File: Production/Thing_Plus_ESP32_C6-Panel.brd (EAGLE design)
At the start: 89.7 x 72.6 mm, 363 parts, among them J1 THING_PLUS_LOGICAL, J10 MICRO-SDFRICTION, J11 THING_PLUS_LOGICAL, J14 QWIIC_RIGHT_ANGLE, J15 MICRO-SDFRICTION, J4 QWIIC_RIGHT_ANGLE, J5 MICRO-SDFRICTION, J6 THING_PLUS_LOGICAL, J9 QWIIC_RIGHT_ANGLE, Q1 20V/4.2A/52mΩ/1.4W, Q2 20V/4.2A/52mΩ/1.4W, Q3 20V/4.2A/52mΩ/1.4W, Q4 20V/4.2A/52mΩ/1.4W, Q5 20V/4.2A/52mΩ/1.4W, Q6 20V/4.2A/52mΩ/1.4W, U1 ESP32-C6-WROOM-1-NARROW, U10 RT9080-33GJ5, U11 MCP73831, U12 MAX17048, U2 RT9080-33GJ5, U3 MCP73831, U4 MAX17048, U5 ESP32-C6-WROOM-1-NARROW, U6 RT9080-33GJ5, U7 MCP73831, U8 MAX17048, U9 ESP32-C6-WROOM-1-NARROW

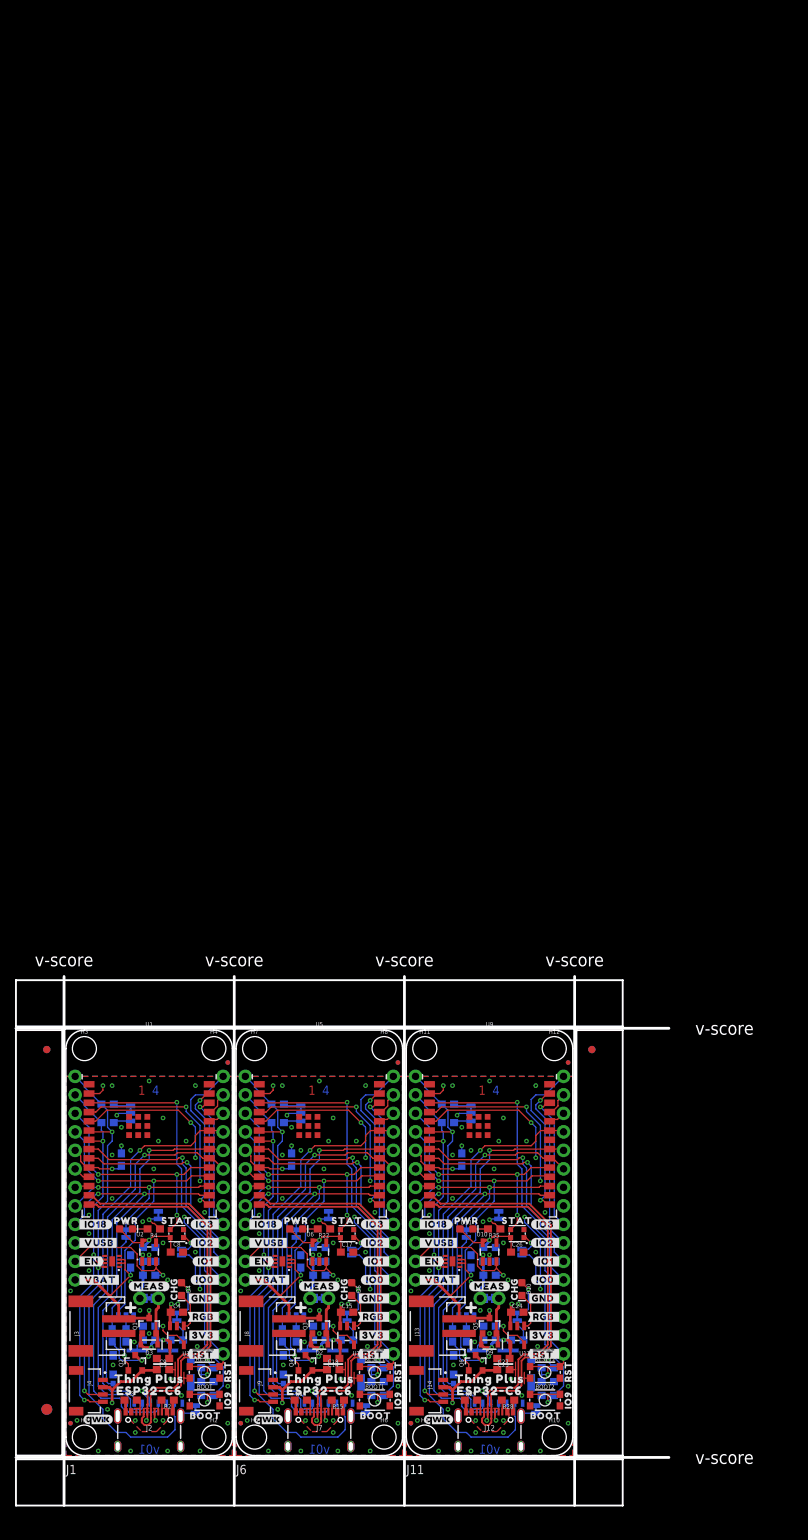
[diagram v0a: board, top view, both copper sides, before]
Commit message: Add v10 panel files
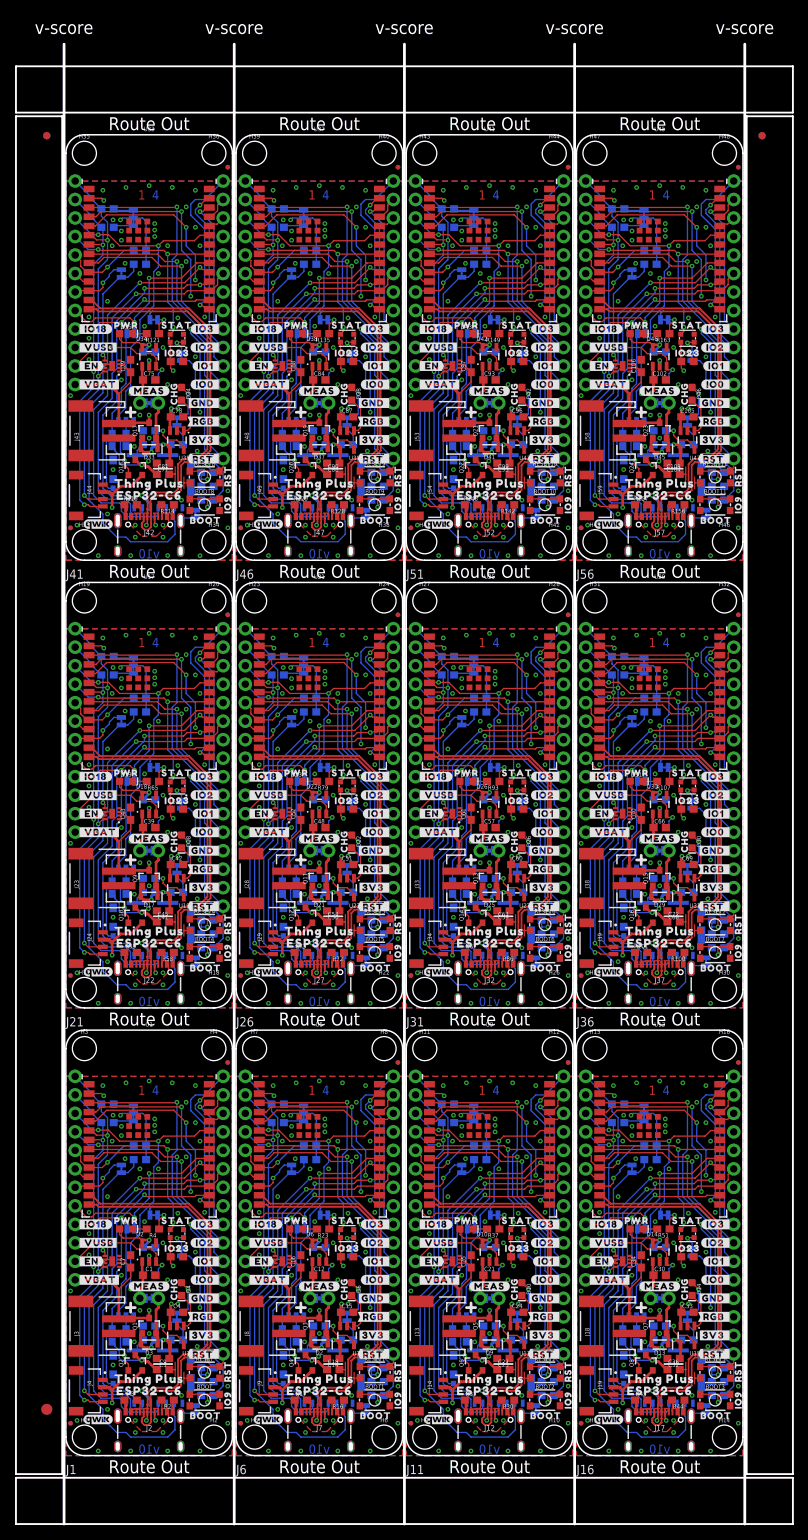
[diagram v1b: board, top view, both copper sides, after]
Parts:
- added ALRT, ALRT1, ALRT10, ALRT11, ALRT2, ALRT3, ALRT4, ALRT5, ALRT6, ALRT7, ALRT8, ALRT9, CHG10, CHG11, CHG3, CHG4, CHG5, CHG6, CHG7, CHG8, CHG9, PWR10, PWR11, PWR3, PWR4, PWR5, PWR6, PWR7, PWR8, PWR9, RGB10, RGB11, RGB3, RGB4, RGB5, RGB6, RGB7, RGB8, RGB9, SD_DET10, SD_DET11, SD_DET3, SD_DET4, SD_DET5, SD_DET6, SD_DET7, SD_DET8, SD_DET9, SHLD10, SHLD11, SHLD3, SHLD4, SHLD5, SHLD6, SHLD7, SHLD8, SHLD9: JUMPER-SMT_2_NC_TRACE_SILK, SparkFun-Jumpers:SMT-JUMPER_2_NC_TRACE_SILK
- added BOOT10, BOOT11, BOOT3, BOOT4, BOOT5, BOOT6, BOOT7, BOOT8, BOOT9, RESET10, RESET11, RESET3, RESET4, RESET5, RESET6, RESET7, RESET8, RESET9: MOMENTARY-SWITCH-SPST-SMD-4.6X2.8MM, SparkFun-Switches:TACTILE_SWITCH_SMD_4.6X2.8MM
- added C100, C101, C106, C107, C28, C29, C34, C35, C37, C38, C43, C44, C46, C47, C52, C53, C55, C56, C61, C62, C64, C65, C70, C71, C73, C74, C79, C80, C82, C83, C88, C89, C91, C92, C97, C98: 0.1uF, SparkFun-Capacitors:0603
- added C102, C103, C104, C105, C30, C31, C32, C33, C39, C40, C41, C42, C48, C49, C50, C51, C57, C58, C59, C60, C66, C67, C68, C69, C75, C76, C77, C78, C84, C85, C86, C87, C93, C94, C95, C96: 2.2uF, SparkFun-Capacitors:0603
- added C108, C36, C45, C54, C63, C72, C81, C90, C99: 10uF, SparkFun-Capacitors:0603
- added D13, D17, D21, D25, D29, D33, D37, D41, D45: 1A/23V/620mV, SparkFun-DiscreteSemi:SOD-323
- added D14, D18, D22, D26, D30, D34, D38, D42, D46: Yellow, SparkFun-LED:LED-0603
- added D15, D19, D23, D27, D31, D35, D39, D43, D47: (no value), SparkFun-LED:LED-0603
- added D16, D20, D24, D28, D32, D36, D40, D44, D48: WS2812_2020, SparkFun-LED:WS2812-2020
- added FD13, FD14, FD15, FD16, FD17, FD18, FD19, FD20, FD21, FD22, FD23, FD24, FD25, FD26, FD27, FD28, FD29, FD30, FD31, FD32, FD33, FD34, FD35, FD36, FD37, FD38, FD39, FD40, FD41, FD42, FD43, FD44, FD45, FD46, FD47, FD48: FIDUCIALUFIDUCIAL, SparkFun-Aesthetics:FIDUCIAL-MICRO
- added H13, H14, H15, H16, H17, H18, H19, H20, H21, H22, H23, H24, H25, H26, H27, H28, H29, H30, H31, H32, H33, H34, H35, H36, H37, H38, H39, H40, H41, H42, H43, H44, H45, H46, H47, H48: STAND-OFF, SparkFun-Hardware:STAND-OFF
- added I2C10, I2C11, I2C3, I2C4, I2C5, I2C6, I2C7, I2C8, I2C9: JUMPER-SMT_3_2-NC_TRACE_SILK, SparkFun-Jumpers:SMT-JUMPER_3_2-NC_TRACE_SILK
- added J16, J21, J26, J31, J36, J41, J46, J51, J56: THING_PLUS_LOGICAL, SparkFun-Boards:THING_PLUS
- added J17, J22, J27, J32, J37, J42, J47, J52, J57: (no value), SparkFun-Connectors:USB-C-16P_4LAYER-PADS
- added J18, J23, J28, J33, J38, J43, J48, J53, J58: (no value), SparkFun-Connectors:JST-2-SMD
- added J19, J24, J29, J34, J39, J44, J49, J54, J59: QWIIC_RIGHT_ANGLE, SparkFun-Connectors:JST04_1MM_RA
- added J20, J25, J30, J35, J40, J45, J50, J55, J60: MICRO-SDFRICTION, SparkFun-Connectors:MICROSD_TINY
- added LOGO10, LOGO13, LOGO16, LOGO19, LOGO22, LOGO25, LOGO28, LOGO31, LOGO34: SFE_LOGO_NAME_FLAME.1_INCH, SparkFun-Aesthetics:SFE_LOGO_NAME_FLAME_.1
- added LOGO11, LOGO14, LOGO17, LOGO20, LOGO23, LOGO26, LOGO29, LOGO32, LOGO35: QWIIC_LOGO_4MM, SparkFun-Aesthetics:QWIIC_4MM
- added LOGO12, LOGO15, LOGO18, LOGO21, LOGO24, LOGO27, LOGO30, LOGO33, LOGO36: OSHW-LOGOM, SparkFun-Aesthetics:OSHW-LOGO-M
- added LP10, LP11, LP3, LP4, LP5, LP6, LP7, LP8, LP9: JUMPER-SMT_3_1-NC_TRACE_SILK, SparkFun-Jumpers:SMT-JUMPER_3_1-NC_TRACE_SILK
- added MEAS10, MEAS11, MEAS3, MEAS4, MEAS5, MEAS6, MEAS7, MEAS8, MEAS9: JUMPER-COMBO_2_NC_TRACE, SparkFun-Jumpers:COMBO-JUMPER_2_NC_TRACE
- added Q10, Q11, Q12, Q13, Q14, Q15, Q16, Q17, Q18, Q19, Q20, Q21, Q22, Q23, Q24, Q7, Q8, Q9: 20V/4.2A/52mΩ/1.4W, SparkFun-DiscreteSemi:SOT23-3
- added R100, R101, R114, R115, R128, R129, R142, R143, R156, R157, R44, R45, R58, R59, R72, R73, R86, R87: 5.1k, SparkFun-Resistors:0603
- added R102, R103, R104, R110, R111, R112, R113, R116, R117, R118, R124, R125, R126, R127, R130, R131, R132, R138, R139, R140, R141, R144, R145, R146, R152, R153, R154, R155, R158, R159, R160, R166, R167, R168, R40, R41, R42, R43, R46, R47, R48, R54, R55, R56, R57, R60, R61, R62, R68, R69, R70, R71, R74, R75, R76, R82, R83, R84, R85, R88, R89, R90, R96, R97, R98, R99: 100k, SparkFun-Resistors:0603
- added R105, R106, R107, R119, R120, R121, R133, R134, R135, R147, R148, R149, R161, R162, R163, R49, R50, R51, R63, R64, R65, R77, R78, R79, R91, R92, R93: 4.7k, SparkFun-Resistors:0603
- added R108, R109, R122, R123, R136, R137, R150, R151, R164, R165, R52, R53, R66, R67, R80, R81, R94, R95: 2.2k, SparkFun-Resistors:0603
- added U$184, U$247, U$310, U$373, U$436, U$499, U$562, U$625, U$688, U$751: (no value), output:#_IO21#POCI#0
- added U$185, U$248, U$311, U$374, U$437, U$500, U$563, U$626, U$689, U$752: (no value), output:#_IO19#SCK#0
- added U$186, U$249, U$312, U$375, U$438, U$501, U$564, U$627, U$690, U$753: (no value), output:#_IO20#PICO#0
- added U$187, U$250, U$313, U$376, U$439, U$502, U$565, U$628, U$691, U$754: (no value), output:#LP#0
- added U$188, U$251, U$314, U$377, U$440, U$503, U$566, U$629, U$692, U$755: (no value), output:#IO15#0
- added U$189, U$252, U$315, U$378, U$441, U$504, U$567, U$630, U$693, U$756: (no value), output:#ALRT#0
- added U$190, U$253, U$316, U$379, U$442, U$505, U$568, U$631, U$694: (no value), output:#SHLD#0
- added U$191, U$254, U$317, U$380, U$443, U$506, U$569, U$632, U$695: (no value), output:#I�C#0
- added U$192, U$255, U$318, U$381, U$444, U$507, U$570, U$633, U$696: (no value), output:#_IO18#0
- added U$193, U$256, U$319, U$382, U$445, U$508, U$571, U$634, U$697: (no value), output:#_VUSB#0
- added U$194, U$257, U$320, U$383, U$446, U$509, U$572, U$635, U$698: (no value), output:#_VBAT#0
- added U$195, U$258, U$321, U$384, U$447, U$510, U$573, U$636, U$699: (no value), output:#_EN#0
- added U$196, U$259, U$322, U$385, U$448, U$511, U$574, U$637, U$700: (no value), output:#IO3_#0
- added U$197, U$260, U$323, U$386, U$449, U$512, U$575, U$638, U$701: (no value), output:#IO2_#0
- added U$198, U$261, U$324, U$387, U$450, U$513, U$576, U$639, U$702: (no value), output:#IO1_#0
- added U$199, U$262, U$325, U$388, U$451, U$514, U$577, U$640, U$703: (no value), output:#IO0_#0
- added U$200, U$263, U$326, U$389, U$452, U$515, U$578, U$641, U$704: (no value), output:#GND_#0
- added U$201, U$264, U$327, U$390, U$453, U$516, U$579, U$642, U$705: (no value), output:#3V3_#0
- added U$202, U$223, U$265, U$286, U$328, U$349, U$391, U$412, U$454, U$475, U$517, U$538, U$580, U$601, U$643, U$664, U$706, U$727: (no value), output:##RST#_#0
- added U$203, U$266, U$329, U$392, U$455, U$518, U$581, U$644, U$707: (no value), output:#SDA#IO6_#0
- added U$204, U$267, U$330, U$393, U$456, U$519, U$582, U$645, U$708: (no value), output:#SCL#IO7_#0
- added U$205, U$268, U$331, U$394, U$457, U$520, U$583, U$646, U$709: (no value), output:#IO8_#0
- added U$206, U$269, U$332, U$395, U$458, U$521, U$584, U$647, U$710: (no value), output:#IO10_#0
- added U$207, U$270, U$333, U$396, U$459, U$522, U$585, U$648, U$711: (no value), output:#IO11_#0
- added U$208, U$271, U$334, U$397, U$460, U$523, U$586, U$649, U$712: (no value), output:#IO18_#0
- added U$209, U$272, U$335, U$398, U$461, U$524, U$587, U$650, U$713: (no value), output:#_IO9#0
- added U$210, U$273, U$336, U$399, U$462, U$525, U$588, U$651, U$714: (no value), output:#_IO16#TX#0
- added U$211, U$274, U$337, U$400, U$463, U$526, U$589, U$652, U$715: (no value), output:#_IO17#RX#0
- added U$212, U$275, U$338, U$401, U$464, U$527, U$590, U$653, U$716: (no value), output:#_IO5#0
- added U$213, U$276, U$339, U$402, U$465, U$528, U$591, U$654, U$717: (no value), output:#_IO4#0
- added U$214, U$277, U$340, U$403, U$466, U$529, U$592, U$655, U$718: (no value), output:#_IO3#0
- added U$215, U$278, U$341, U$404, U$467, U$530, U$593, U$656, U$719: (no value), output:#_IO2#0
- added U$216, U$279, U$342, U$405, U$468, U$531, U$594, U$657, U$720: (no value), output:#_IO1#0
- added U$217, U$280, U$343, U$406, U$469, U$532, U$595, U$658, U$721: (no value), output:#_IO0#0
- added U$218, U$281, U$344, U$407, U$470, U$533, U$596, U$659, U$722: (no value), output:#_GND#0
- added U$219, U$282, U$345, U$408, U$471, U$534, U$597, U$660, U$723: (no value), output:#_3V3#0
- added U$220, U$283, U$346, U$409, U$472, U$535, U$598, U$661, U$724: (no value), output:#VUSB_#0
- added U$221, U$284, U$347, U$410, U$473, U$536, U$599, U$662, U$725: (no value), output:#VBAT_#0
- added U$222, U$285, U$348, U$411, U$474, U$537, U$600, U$663, U$726: (no value), output:#EN_#0
- added U$224, U$287, U$350, U$413, U$476, U$539, U$602, U$665, U$728: (no value), output:#SD_DET#0
- added U$225, U$288, U$351, U$414, U$477, U$540, U$603, U$666, U$729: (no value), output:BOOT0
- added U$226, U$289, U$352, U$415, U$478, U$541, U$604, U$667, U$730: (no value), output:RST0
- added U$227, U$290, U$353, U$416, U$479, U$542, U$605, U$668, U$731: (no value), output:IO90
- added U$228, U$230, U$291, U$293, U$354, U$356, U$417, U$419, U$480, U$482, U$543, U$545, U$606, U$608, U$669, U$671, U$732, U$734: (no value), output:THING_PLUS0
- added U$229, U$231, U$292, U$294, U$355, U$357, U$418, U$420, U$481, U$483, U$544, U$546, U$607, U$609, U$670, U$672, U$733, U$735: (no value), output:ESP32#C60
- added U$232, U$233, U$295, U$296, U$358, U$359, U$421, U$422, U$484, U$485, U$547, U$548, U$610, U$611, U$673, U$674, U$736, U$737: (no value), output:#MEAS#0
- added U$234, U$297, U$360, U$423, U$486, U$549, U$612, U$675, U$738: (no value), output:#CHG#0
- added U$235, U$298, U$361, U$424, U$487, U$550, U$613, U$676, U$739: (no value), output:#PWR#0
- added U$236, U$299, U$362, U$425, U$488, U$551, U$614, U$677, U$740: (no value), output:PWR0
- added U$237, U$300, U$363, U$426, U$489, U$552, U$615, U$678, U$741: (no value), output:CHG0
- added U$238, U$301, U$364, U$427, U$490, U$553, U$616, U$679, U$742: (no value), output:STAT0
- added U$239, U$302, U$365, U$428, U$491, U$554, U$617, U$680, U$743: (no value), output:#RGB#0
- added U$240, U$303, U$366, U$429, U$492, U$555, U$618, U$681, U$744: (no value), output:#RGB_#0
- added U$241, U$304, U$367, U$430, U$493, U$556, U$619, U$682, U$745: (no value), output:#_RGB#0
- added U$242, U$305, U$368, U$431, U$494, U$557, U$620, U$683, U$746: (no value), output:#G#0
- added U$243, U$306, U$369, U$432, U$495, U$558, U$621, U$684, U$747: (no value), output:IO230
- added U$244, U$307, U$370, U$433, U$496, U$559, U$622, U$685, U$748: (no value), output:#IO15_#0
- added U$245, U$308, U$371, U$434, U$497, U$560, U$623, U$686, U$749: (no value), output:#IO23_#0
- added U$246, U$309, U$372, U$435, U$498, U$561, U$624, U$687, U$750: (no value), output:#IO22_#0
- added U13, U17, U21, U25, U29, U33, U37, U41, U45: ESP32-C6-WROOM-1-NARROW, ESP32-C6-WROOM-1:ESP32-C6-WROOM-1-NARROW
- added U14, U18, U22, U26, U30, U34, U38, U42, U46: RT9080-33GJ5, SparkFun-IC-Power:SOT23-5
- added U15, U19, U23, U27, U31, U35, U39, U43, U47: MCP73831, SparkFun-IC-Power:SOT23-5
- added U16, U20, U24, U28, U32, U36, U40, U44, U48: MAX17048, SparkFun-IC-Power:DFN-8
- R15, R28, R29: value 5.1k -> 100k
- R17, R30, R31: value 100k -> 5.1k
- R20, R33, R34: value 4.7k -> 100k
- R23, R36, R37: value 2.2k -> 4.7k
- R25, R38, R39: value 100k -> 2.2k
- RGB, RGB1, RGB2: value JUMPER-SMT_2_NO_SILK -> JUMPER-SMT_2_NC_TRACE_SILK; device SparkFun-Jumpers:SMT-JUMPER_2_NO_SILK -> SparkFun-Jumpers:SMT-JUMPER_2_NC_TRACE_SILK
- U$100: device output:#EN_#0 -> output:RST0
- U$101: device output:##RST#_#0 -> output:IO90
- U$102: device output:#SD_DET#0 -> output:THING_PLUS0
- U$103: device output:BOOT0 -> output:ESP32#C60
- U$104, U$165: device output:RST0 -> output:THING_PLUS0
- U$105, U$166: device output:IO90 -> output:ESP32#C60
- U$106, U$169: device output:THING_PLUS0 -> output:#MEAS#0
- U$107, U$170: device output:ESP32#C60 -> output:#MEAS#0
- U$108: device output:THING_PLUS0 -> output:#CHG#0
- U$109: device output:ESP32#C60 -> output:#PWR#0
- U$110: device output:#MEAS#0 -> output:PWR0
- U$111: device output:#MEAS#0 -> output:CHG0
- U$112: device output:#CHG#0 -> output:STAT0
- U$113: device output:#PWR#0 -> output:#RGB#0
- U$114: device output:PWR0 -> output:#RGB_#0
- U$115: device output:CHG0 -> output:#_RGB#0
- U$116: device output:STAT0 -> output:#G#0
- U$117: device output:#RGB#0 -> output:IO230
- U$118: device output:#RGB_#0 -> output:#IO15_#0
- U$119: device output:#_RGB#0 -> output:#IO23_#0
- U$120: device output:#SD_P#0 -> output:#IO22_#0
- U$121: device output:#IO20#0 -> output:#_IO21#POCI#0
- U$122: device output:#G#0 -> output:#_IO19#SCK#0
- U$123: device output:#SHLD#0 -> output:#_IO20#PICO#0
- U$124: device output:#I�C#0 -> output:#LP#0
- U$125: device output:#_IO18#0 -> output:#IO15#0
- U$126: device output:#_VUSB#0 -> output:#ALRT#0
- U$127: device output:#_VBAT#0 -> output:#SHLD#0
- U$128: device output:#_EN#0 -> output:#I�C#0
- U$129: device output:#IO3_#0 -> output:#_IO18#0
- U$130: device output:#IO2_#0 -> output:#_VUSB#0
- U$131: device output:#IO1_#0 -> output:#_VBAT#0
- U$132: device output:#IO0_#0 -> output:#_EN#0
- U$133: device output:#GND_#0 -> output:#IO3_#0
- U$134: device output:#3V3_#0 -> output:#IO2_#0
- U$135: device output:##RST#_#0 -> output:#IO1_#0
- U$136: device output:#SDA#IO6_#0 -> output:#IO0_#0
- U$137: device output:#SCL#IO7_#0 -> output:#GND_#0
- U$138: device output:#IO21_#0 -> output:#3V3_#0
- U$139: device output:#IO20_#0 -> output:##RST#_#0
- U$140: device output:#IO8_#0 -> output:#SDA#IO6_#0
- U$141: device output:#IO10_#0 -> output:#SCL#IO7_#0
- U$142: device output:#IO11_#0 -> output:#IO8_#0
- U$143: device output:#IO19_#0 -> output:#IO10_#0
- U$144: device output:#IO18_#0 -> output:#IO11_#0
- U$145: device output:#_IO9#0 -> output:#IO18_#0
- U$146: device output:#_IO16#TX#0 -> output:#_IO9#0
- U$147: device output:#_IO17#RX#0 -> output:#_IO16#TX#0
- U$148: device output:#_IO15#POCI#0 -> output:#_IO17#RX#0
- U$149: device output:#_IO23#PICO#0 -> output:#_IO5#0
- U$150: device output:#_IO22#SCK#0 -> output:#_IO4#0
- U$151: device output:#_IO5#0 -> output:#_IO3#0
- U$152: device output:#_IO4#0 -> output:#_IO2#0
- U$153: device output:#_IO3#0 -> output:#_IO1#0
- U$154: device output:#_IO2#0 -> output:#_IO0#0
- U$155: device output:#_IO1#0 -> output:#_GND#0
- U$156: device output:#_IO0#0 -> output:#_3V3#0
- U$157: device output:#_GND#0 -> output:#VUSB_#0
- U$158: device output:#_3V3#0 -> output:#VBAT_#0
- U$159: device output:#VUSB_#0 -> output:#EN_#0
- U$16: device output:#IO21_#0 -> output:#_IO21#POCI#0
- U$160: device output:#VBAT_#0 -> output:##RST#_#0
- U$161: device output:#EN_#0 -> output:#SD_DET#0
- U$162: device output:##RST#_#0 -> output:BOOT0
- U$163: device output:#SD_DET#0 -> output:RST0
- U$164: device output:BOOT0 -> output:IO90
- U$17: device output:#IO20_#0 -> output:#LP#0
- U$171: device output:#MEAS#0 -> output:#CHG#0
- U$172: device output:#MEAS#0 -> output:#PWR#0
- U$173: device output:#CHG#0 -> output:PWR0
- U$174: device output:#PWR#0 -> output:CHG0
- U$175: device output:PWR0 -> output:STAT0
- U$176: device output:CHG0 -> output:#RGB#0
- U$177: device output:STAT0 -> output:#RGB_#0
- U$178: device output:#RGB#0 -> output:#_RGB#0
- U$179: device output:#RGB_#0 -> output:#G#0
- U$180: device output:#_RGB#0 -> output:IO230
- U$181: device output:#SD_P#0 -> output:#IO15_#0
- U$182: device output:#IO20#0 -> output:#IO23_#0
- U$183: device output:#G#0 -> output:#IO22_#0
- U$21: device output:#IO19_#0 -> output:#_IO19#SCK#0
- U$26: device output:#_IO15#POCI#0 -> output:#_IO20#PICO#0
- U$27: device output:#_IO23#PICO#0 -> output:#IO15#0
- U$28: device output:#_IO22#SCK#0 -> output:#ALRT#0
- U$60: device output:#SD_P#0 -> output:#I�C#0
- U$61: device output:#IO20#0 -> output:#_IO18#0
- U$62: device output:#I�C#0 -> output:IO230
- U$64: device output:#_IO18#0 -> output:#IO23_#0
- U$65: device output:#_VUSB#0 -> output:#IO15_#0
- U$66: device output:#_VBAT#0 -> output:#IO22_#0
- U$67: device output:#_EN#0 -> output:#_VUSB#0
- U$68: device output:#IO3_#0 -> output:#_VBAT#0
- U$69: device output:#IO2_#0 -> output:#_EN#0
- U$70: device output:#IO1_#0 -> output:#IO3_#0
- U$71: device output:#IO0_#0 -> output:#IO2_#0
- U$72: device output:#GND_#0 -> output:#IO1_#0
- U$73: device output:#3V3_#0 -> output:#IO0_#0
- U$74: device output:##RST#_#0 -> output:#GND_#0
- U$75: device output:#SDA#IO6_#0 -> output:#3V3_#0
- U$76: device output:#SCL#IO7_#0 -> output:##RST#_#0
- U$77: device output:#IO21_#0 -> output:#SDA#IO6_#0
- U$78: device output:#IO20_#0 -> output:#SCL#IO7_#0
- U$82: device output:#IO19_#0 -> output:#IO18_#0
- U$83: device output:#IO18_#0 -> output:#_IO9#0
- U$84: device output:#_IO9#0 -> output:#_IO16#TX#0
- U$85: device output:#_IO16#TX#0 -> output:#_IO17#RX#0
- U$86: device output:#_IO17#RX#0 -> output:#_IO5#0
- U$87: device output:#_IO15#POCI#0 -> output:#_IO4#0
- U$88: device output:#_IO23#PICO#0 -> output:#_IO3#0
- U$89: device output:#_IO22#SCK#0 -> output:#_IO2#0
- U$90: device output:#_IO5#0 -> output:#_IO1#0
- U$91: device output:#_IO4#0 -> output:#_IO0#0
- U$92: device output:#_IO3#0 -> output:#_GND#0
- U$93: device output:#_IO2#0 -> output:#_3V3#0
- U$94: device output:#_IO1#0 -> output:#VUSB_#0
- U$95: device output:#_IO0#0 -> output:#VBAT_#0
- U$96: device output:#_GND#0 -> output:#EN_#0
- U$97: device output:#_3V3#0 -> output:##RST#_#0
- U$98: device output:#VUSB_#0 -> output:#SD_DET#0
- U$99: device output:#VBAT_#0 -> output:BOOT0
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- renumbered SD_P to LP, SD_P1 to LP1, SD_P2 to LP2
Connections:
- net IO18/SD_CS renamed IO18/!CS!
- net IO18/SD_CS1 renamed IO18/!CS!1
- net IO18/SD_CS2 renamed IO18/!CS!2
- removed net IO15/POCI: J1.16, J5.7, U1.23
- removed net IO15/POCI1: J10.7, J6.16, U5.23
- removed net IO15/POCI2: J11.16, J15.7, U9.23
- removed net IO19/SD_DET: J1.8, SD_DET.2, U1.17
- removed net IO19/SD_DET1: J6.8, SD_DET1.2, U5.17
- removed net IO19/SD_DET2: J11.8, SD_DET2.2, U9.17
- removed net IO20/SD_POW: J1.4, LP.1, U1.18
- removed net IO20/SD_POW1: J6.4, LP1.1, U5.18
- removed net IO20/SD_POW2: J11.4, LP2.1, U9.18
- removed net IO21/STAT: D5.DI, J1.3, U1.19
- removed net IO21/STAT1: D8.DI, J6.3, U5.19
- removed net IO21/STAT2: D12.DI, J11.3, U9.19
- removed net IO22/SCK: J1.18, J5.5, U1.20
- removed net IO22/SCK1: J10.5, J6.18, U5.20
- removed net IO22/SCK2: J11.18, J15.5, U9.20
- removed net IO23/PICO: J1.17, J5.3, U1.21
- removed net IO23/PICO1: J10.3, J6.17, U5.21
- removed net IO23/PICO2: J11.17, J15.3, U9.21
- new net 3.3V10: C94.1, D43.A, I2C10.2, J51.27, J54.2, Q22.2, R141.2, R144.2, R153.2, R154.2, U41.2, U42.5
- new net 3.3V11: C103.1, D47.A, I2C11.2, J56.27, J59.2, Q24.2, R155.2, R158.2, R167.2, R168.2, U45.2, U46.5
- new net 3.3V3: C31.1, D15.A, I2C3.2, J16.27, J19.2, Q8.2, R43.2, R46.2, R55.2, R56.2, U13.2, U14.5
- new net 3.3V4: C40.1, D19.A, I2C4.2, J21.27, J24.2, Q10.2, R57.2, R60.2, R69.2, R70.2, U17.2, U18.5
- new net 3.3V5: C49.1, D23.A, I2C5.2, J26.27, J29.2, Q12.2, R71.2, R74.2, R83.2, R84.2, U21.2, U22.5
- new net 3.3V6: C58.1, D27.A, I2C6.2, J31.27, J34.2, Q14.2, R85.2, R88.2, R97.2, R98.2, U25.2, U26.5
- new net 3.3V7: C67.1, D31.A, I2C7.2, J36.27, J39.2, Q16.2, R102.2, R111.2, R112.2, R99.2, U29.2, U30.5
- new net 3.3V8: C76.1, D35.A, I2C8.2, J41.27, J44.2, Q18.2, R113.2, R116.2, R125.2, R126.2, U33.2, U34.5
- new net 3.3V9: C85.1, D39.A, I2C9.2, J46.27, J49.2, Q20.2, R127.2, R130.2, R139.2, R140.2, U37.2, U38.5
- new net ESP_EN10: C91.1, J51.28, R144.1, RESET10.3, RESET10.4, U41.3
- new net ESP_EN11: C100.1, J56.28, R158.1, RESET11.3, RESET11.4, U45.3
- new net ESP_EN3: C28.1, J16.28, R46.1, RESET3.3, RESET3.4, U13.3
- new net ESP_EN4: C37.1, J21.28, R60.1, RESET4.3, RESET4.4, U17.3
- new net ESP_EN5: C46.1, J26.28, R74.1, RESET5.3, RESET5.4, U21.3
- new net ESP_EN6: C55.1, J31.28, R88.1, RESET6.3, RESET6.4, U25.3
- new net ESP_EN7: C64.1, J36.28, R102.1, RESET7.3, RESET7.4, U29.3
- new net ESP_EN8: C73.1, J41.28, R116.1, RESET8.3, RESET8.4, U33.3
- new net ESP_EN9: C82.1, J46.28, R130.1, RESET9.3, RESET9.4, U37.3
- new net GND10: BOOT10.1, BOOT10.2, C91.2, C92.2, C93.2, C94.2, C95.2, C96.2, C97.2, C98.2, C99.2, D44.GND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
- new net GND11: BOOT11.1, BOOT11.2, C100.2, C101.2, C102.2, C103.2, C104.2, C105.2, C106.2, C107.2, C108.2, D48.GND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
- new net GND3: BOOT3.1, BOOT3.2, C28.2, C29.2, C30.2, C31.2, C32.2, C33.2, C34.2, C35.2, C36.2, D16.GND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
- new net GND4: BOOT4.1, BOOT4.2, C37.2, C38.2, C39.2, C40.2, C41.2, C42.2, C43.2, C44.2, C45.2, D20.GND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
- new net GND5: BOOT5.1, BOOT5.2, C46.2, C47.2, C48.2, C49.2, C50.2, C51.2, C52.2, C53.2, C54.2, D24.GND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
- new net GND6: BOOT6.1, BOOT6.2, C55.2, C56.2, C57.2, C58.2, C59.2, C60.2, C61.2, C62.2, C63.2, D28.GND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
- new net GND7: BOOT7.1, BOOT7.2, C64.2, C65.2, C66.2, C67.2, C68.2, C69.2, C70.2, C71.2, C72.2, D32.GND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
- new net GND8: BOOT8.1, BOOT8.2, C73.2, C74.2, C75.2, C76.2, C77.2, C78.2, C79.2, C80.2, C81.2, D36.GND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
- new net GND9: BOOT9.1, BOOT9.2, C82.2, C83.2, C84.2, C85.2, C86.2, C87.2, C88.2, C89.2, C90.2, D40.GND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
- new net IO11/!ALRT!: ALRT.2, J1.7, U1.12
- new net IO11/!ALRT!1: ALRT1.2, J6.7, U5.12
- new net IO11/!ALRT!10: ALRT10.2, J51.7, U41.12
- new net IO11/!ALRT!11: ALRT11.2, J56.7, U45.12
- new net IO11/!ALRT!2: ALRT2.2, J11.7, U9.12
- new net IO11/!ALRT!3: ALRT3.2, J16.7, U13.12
- new net IO11/!ALRT!4: ALRT4.2, J21.7, U17.12
- new net IO11/!ALRT!5: ALRT5.2, J26.7, U21.12
- new net IO11/!ALRT!6: ALRT6.2, J31.7, U25.12
- new net IO11/!ALRT!7: ALRT7.2, J36.7, U29.12
- new net IO11/!ALRT!8: ALRT8.2, J41.7, U33.12
- new net IO11/!ALRT!9: ALRT9.2, J46.7, U37.12
- new net IO15/LP: J1.3, LP.1, U1.23
- new net IO15/LP1: J6.3, LP1.1, U5.23
- new net IO15/LP10: J51.3, LP10.1, U41.23
- new net IO15/LP11: J56.3, LP11.1, U45.23
- new net IO15/LP2: J11.3, LP2.1, U9.23
- new net IO15/LP3: J16.3, LP3.1, U13.23
- new net IO15/LP4: J21.3, LP4.1, U17.23
- new net IO15/LP5: J26.3, LP5.1, U21.23
- new net IO15/LP6: J31.3, LP6.1, U25.23
- new net IO15/LP7: J36.3, LP7.1, U29.23
- new net IO15/LP8: J41.3, LP8.1, U33.23
- new net IO15/LP9: J46.3, LP9.1, U37.23
- new net IO16/TX10: J51.14, U41.25
- new net IO16/TX11: J56.14, U45.25
- new net IO16/TX3: J16.14, U13.25
- new net IO16/TX4: J21.14, U17.25
- new net IO16/TX5: J26.14, U21.25
- new net IO16/TX6: J31.14, U25.25
- new net IO16/TX7: J36.14, U29.25
- new net IO16/TX8: J41.14, U33.25
- new net IO16/TX9: J46.14, U37.25
- new net IO17/RX10: J51.15, U41.24
- new net IO17/RX11: J56.15, U45.24
- new net IO17/RX3: J16.15, U13.24
- new net IO17/RX4: J21.15, U17.24
- new net IO17/RX5: J26.15, U21.24
- new net IO17/RX6: J31.15, U25.24
- new net IO17/RX7: J36.15, U29.24
- new net IO17/RX8: J41.15, U33.24
- new net IO17/RX9: J46.15, U37.24
- new net IO18/!CS!10: J51.9, J55.2, U41.16
- new net IO18/!CS!11: J56.9, J60.2, U45.16
- new net IO18/!CS!3: J16.9, J20.2, U13.16
- new net IO18/!CS!4: J21.9, J25.2, U17.16
- new net IO18/!CS!5: J26.9, J30.2, U21.16
- new net IO18/!CS!6: J31.9, J35.2, U25.16
- new net IO18/!CS!7: J36.9, J40.2, U29.16
- new net IO18/!CS!8: J41.9, J45.2, U33.16
- new net IO18/!CS!9: J46.9, J50.2, U37.16
- new net IO19/SCK: J1.18, J5.5, U1.17
- new net IO19/SCK1: J10.5, J6.18, U5.17
- new net IO19/SCK10: J51.18, J55.5, U41.17
- new net IO19/SCK11: J56.18, J60.5, U45.17
- new net IO19/SCK2: J11.18, J15.5, U9.17
- new net IO19/SCK3: J16.18, J20.5, U13.17
- new net IO19/SCK4: J21.18, J25.5, U17.17
- new net IO19/SCK5: J26.18, J30.5, U21.17
- new net IO19/SCK6: J31.18, J35.5, U25.17
- new net IO19/SCK7: J36.18, J40.5, U29.17
- new net IO19/SCK8: J41.18, J45.5, U33.17
- new net IO19/SCK9: J46.18, J50.5, U37.17
- new net IO20/PICO: J1.17, J5.3, U1.18
- new net IO20/PICO1: J10.3, J6.17, U5.18
- new net IO20/PICO10: J51.17, J55.3, U41.18
- new net IO20/PICO11: J56.17, J60.3, U45.18
- new net IO20/PICO2: J11.17, J15.3, U9.18
- new net IO20/PICO3: J16.17, J20.3, U13.18
- new net IO20/PICO4: J21.17, J25.3, U17.18
- new net IO20/PICO5: J26.17, J30.3, U21.18
- new net IO20/PICO6: J31.17, J35.3, U25.18
- new net IO20/PICO7: J36.17, J40.3, U29.18
- new net IO20/PICO8: J41.17, J45.3, U33.18
- new net IO20/PICO9: J46.17, J50.3, U37.18
- new net IO21/POCI: J1.16, J5.7, U1.19
- new net IO21/POCI1: J10.7, J6.16, U5.19
- new net IO21/POCI10: J51.16, J55.7, U41.19
- new net IO21/POCI11: J56.16, J60.7, U45.19
- new net IO21/POCI2: J11.16, J15.7, U9.19
- new net IO21/POCI3: J16.16, J20.7, U13.19
- new net IO21/POCI4: J21.16, J25.7, U17.19
- new net IO21/POCI5: J26.16, J30.7, U21.19
- new net IO21/POCI6: J31.16, J35.7, U25.19
- new net IO21/POCI7: J36.16, J40.7, U29.19
- new net IO21/POCI8: J41.16, J45.7, U33.19
- new net IO21/POCI9: J46.16, J50.7, U37.19
- new net IO22/!SD_DET!: J1.8, SD_DET.2, U1.20
- new net IO22/!SD_DET!1: J6.8, SD_DET1.2, U5.20
- new net IO22/!SD_DET!10: J51.8, SD_DET10.2, U41.20
- new net IO22/!SD_DET!11: J56.8, SD_DET11.2, U45.20
- new net IO22/!SD_DET!2: J11.8, SD_DET2.2, U9.20
- new net IO22/!SD_DET!3: J16.8, SD_DET3.2, U13.20
- new net IO22/!SD_DET!4: J21.8, SD_DET4.2, U17.20
- new net IO22/!SD_DET!5: J26.8, SD_DET5.2, U21.20
- new net IO22/!SD_DET!6: J31.8, SD_DET6.2, U25.20
- new net IO22/!SD_DET!7: J36.8, SD_DET7.2, U29.20
- new net IO22/!SD_DET!8: J41.8, SD_DET8.2, U33.20
- new net IO22/!SD_DET!9: J46.8, SD_DET9.2, U37.20
- new net IO23/STAT: D5.DI, J1.4, U1.21
- new net IO23/STAT1: D8.DI, J6.4, U5.21
- new net IO23/STAT10: D44.DI, J51.4, U41.21
- new net IO23/STAT11: D48.DI, J56.4, U45.21
- new net IO23/STAT2: D12.DI, J11.4, U9.21
- new net IO23/STAT3: D16.DI, J16.4, U13.21
- new net IO23/STAT4: D20.DI, J21.4, U17.21
- new net IO23/STAT5: D24.DI, J26.4, U21.21
- new net IO23/STAT6: D28.DI, J31.4, U25.21
- new net IO23/STAT7: D32.DI, J36.4, U29.21
- new net IO23/STAT8: D36.DI, J41.4, U33.21
- new net IO23/STAT9: D40.DI, J46.4, U37.21
- new net IO27: J16.21, U13.26
- new net IO28: J16.5, R43.1, U13.10
- new net IO29: J16.24, U13.8
- new net IO30: J16.23, U13.9
- new net IO31: J16.6, U13.11
- new net IO32: J21.20, U17.4
- new net IO33: J21.19, U17.5
- new net IO34: J21.22, U17.27
- new net IO35: J21.21, U17.26
- new net IO36: J21.5, R57.1, U17.10
- new net IO37: J21.24, U17.8
- new net IO38: J21.23, U17.9
- new net IO39: J21.6, U17.11
- new net IO40: J26.20, U21.4
- new net IO41: J26.19, U21.5
- new net IO42: J26.22, U21.27
- new net IO43: J26.21, U21.26
- new net IO44: J26.5, R71.1, U21.10
- new net IO45: J26.24, U21.8
- new net IO46: J26.23, U21.9
- new net IO47: J26.6, U21.11
- new net IO48: J31.20, U25.4
- new net IO49: J31.19, U25.5
- new net IO50: J31.22, U25.27
- new net IO51: J31.21, U25.26
- new net IO52: J31.5, R85.1, U25.10
- new net IO53: J31.24, U25.8
- new net IO54: J31.23, U25.9
- new net IO55: J31.6, U25.11
- new net IO56: J36.20, U29.4
- new net IO57: J36.19, U29.5
- new net IO58: J36.22, U29.27
- new net IO59: J36.21, U29.26
- new net IO6/SDA10: J51.1, J54.3, R150.1, U41.6, U44.8
- new net IO6/SDA11: J56.1, J59.3, R164.1, U45.6, U48.8
- new net IO6/SDA3: J16.1, J19.3, R52.1, U13.6, U16.8
- new net IO6/SDA4: J21.1, J24.3, R66.1, U17.6, U20.8
- new net IO6/SDA5: J26.1, J29.3, R80.1, U21.6, U24.8
- new net IO6/SDA6: J31.1, J34.3, R94.1, U25.6, U28.8
- new net IO6/SDA7: J36.1, J39.3, R108.1, U29.6, U32.8
- new net IO6/SDA8: J41.1, J44.3, R122.1, U33.6, U36.8
- new net IO6/SDA9: J46.1, J49.3, R136.1, U37.6, U40.8
- new net IO60: J36.5, R99.1, U29.10
- new net IO61: J36.24, U29.8
- new net IO62: J36.23, U29.9
- new net IO63: J36.6, U29.11
- new net IO64: J41.20, U33.4
- new net IO65: J41.19, U33.5
- new net IO66: J41.22, U33.27
- new net IO67: J41.21, U33.26
- new net IO68: J41.5, R113.1, U33.10
- new net IO69: J41.24, U33.8
- new net IO7/SCL10: J51.2, J54.4, R151.2, U41.7, U44.7
- new net IO7/SCL11: J56.2, J59.4, R165.2, U45.7, U48.7
- new net IO7/SCL3: J16.2, J19.4, R53.2, U13.7, U16.7
- new net IO7/SCL4: J21.2, J24.4, R67.2, U17.7, U20.7
- new net IO7/SCL5: J26.2, J29.4, R81.2, U21.7, U24.7
- new net IO7/SCL6: J31.2, J34.4, R95.2, U25.7, U28.7
- new net IO7/SCL7: J36.2, J39.4, R109.2, U29.7, U32.7
- new net IO7/SCL8: J41.2, J44.4, R123.2, U33.7, U36.7
- new net IO7/SCL9: J46.2, J49.4, R137.2, U37.7, U40.7
- new net IO70: J41.23, U33.9
- new net IO71: J41.6, U33.11
- new net IO72: J46.20, U37.4
- new net IO73: J46.19, U37.5
- new net IO74: J46.22, U37.27
- new net IO75: J46.21, U37.26
- new net IO76: J46.5, R127.1, U37.10
- new net IO77: J46.24, U37.8
- new net IO78: J46.23, U37.9
- new net IO79: J46.6, U37.11
- new net IO80: J51.20, U41.4
- new net IO81: J51.19, U41.5
- new net IO82: J51.22, U41.27
- new net IO83: J51.21, U41.26
- new net IO84: J51.5, R141.1, U41.10
- new net IO85: J51.24, U41.8
- new net IO86: J51.23, U41.9
- new net IO87: J51.6, U41.11
- new net IO88: J56.20, U45.4
- new net IO89: J56.19, U45.5
- new net IO9/BOOT10: BOOT10.3, BOOT10.4, C92.1, J51.13, U41.15
- new net IO9/BOOT11: BOOT11.3, BOOT11.4, C101.1, J56.13, U45.15
- new net IO9/BOOT3: BOOT3.3, BOOT3.4, C29.1, J16.13, U13.15
- new net IO9/BOOT4: BOOT4.3, BOOT4.4, C38.1, J21.13, U17.15
- new net IO9/BOOT5: BOOT5.3, BOOT5.4, C47.1, J26.13, U21.15
- new net IO9/BOOT6: BOOT6.3, BOOT6.4, C56.1, J31.13, U25.15
- new net IO9/BOOT7: BOOT7.3, BOOT7.4, C65.1, J36.13, U29.15
- new net IO9/BOOT8: BOOT8.3, BOOT8.4, C74.1, J41.13, U33.15
- new net IO9/BOOT9: BOOT9.3, BOOT9.4, C83.1, J46.13, U37.15
- new net IO90: J56.22, U45.27
- new net IO91: J56.21, U45.26
- new net IO92: J56.5, R155.1, U45.10
- new net IO93: J56.24, U45.8
- new net IO94: J56.23, U45.9
- new net IO95: J56.6, U45.11
- new net LED_DO10: J51.26, RGB10.1
- new net LED_DO11: J56.26, RGB11.1
- new net LED_DO3: J16.26, RGB3.1
- new net LED_DO4: J21.26, RGB4.1
- new net LED_DO5: J26.26, RGB5.1
- new net LED_DO6: J31.26, RGB6.1
- new net LED_DO7: J36.26, RGB7.1
- new net LED_DO8: J41.26, RGB8.1
- new net LED_DO9: J46.26, RGB9.1
- new net N$100: D26.C, U27.1
- new net N$101: CHG6.1, D26.A
- new net N$102: CHG6.2, R91.1
- new net N$103: R92.2, U27.5
- new net N$104: I2C6.3, R94.2
- new net N$105: I2C6.1, R95.1
- new net N$106: J35.9, R96.1, SD_DET6.1
- new net N$107: D25.C, MEAS6.1, MEAS6.3, Q13.2
- new net N$108: D27.C, R93.2
- new net N$109: PWR6.2, R93.1
- new net N$110: D28.DO, RGB6.2
- new net N$111: LP6.2, Q14.1, R97.1
- new net N$112: ALRT6.1, R98.1, U28.5
- new net N$113: J37.B5, R100.2
- new net N$114: J37.A5, R101.2
- new net N$115: C66.1, MEAS7.2, MEAS7.4, R104.1, U30.1
- new net N$116: D30.C, U31.1
- new net N$117: CHG7.1, D30.A
- new net N$118: CHG7.2, R105.1
- new net N$119: R106.2, U31.5
- new net N$120: I2C7.3, R108.2
- new net N$121: I2C7.1, R109.1
- new net N$122: J40.9, R110.1, SD_DET7.1
- new net N$123: D29.C, MEAS7.1, MEAS7.3, Q15.2
- new net N$124: D31.C, R107.2
- new net N$125: PWR7.2, R107.1
- new net N$126: D32.DO, RGB7.2
- new net N$127: LP7.2, Q16.1, R111.1
- new net N$128: ALRT7.1, R112.1, U32.5
- new net N$129: J42.B5, R114.2
- new net N$130: J42.A5, R115.2
- new net N$131: C75.1, MEAS8.2, MEAS8.4, R118.1, U34.1
- new net N$132: D34.C, U35.1
- new net N$133: CHG8.1, D34.A
- new net N$134: CHG8.2, R119.1
- new net N$135: R120.2, U35.5
- new net N$136: I2C8.3, R122.2
- new net N$137: I2C8.1, R123.1
- new net N$138: J45.9, R124.1, SD_DET8.1
- new net N$139: D33.C, MEAS8.1, MEAS8.3, Q17.2
- new net N$140: D35.C, R121.2
- new net N$141: PWR8.2, R121.1
- new net N$142: D36.DO, RGB8.2
- new net N$143: LP8.2, Q18.1, R125.1
- new net N$144: ALRT8.1, R126.1, U36.5
- new net N$145: J47.B5, R128.2
- new net N$146: J47.A5, R129.2
- new net N$147: C84.1, MEAS9.2, MEAS9.4, R132.1, U38.1
- new net N$148: D38.C, U39.1
- new net N$149: CHG9.1, D38.A
- new net N$150: CHG9.2, R133.1
- new net N$151: R134.2, U39.5
- new net N$152: I2C9.3, R136.2
- new net N$153: I2C9.1, R137.1
- new net N$154: J50.9, R138.1, SD_DET9.1
- new net N$155: D37.C, MEAS9.1, MEAS9.3, Q19.2
- new net N$156: D39.C, R135.2
- new net N$157: PWR9.2, R135.1
- new net N$158: D40.DO, RGB9.2
- new net N$159: LP9.2, Q20.1, R139.1
- new net N$160: ALRT9.1, R140.1, U40.5
- new net N$161: J52.B5, R142.2
- new net N$162: J52.A5, R143.2
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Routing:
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- added copper zone on layer 15, net 3.3V10
- added copper zone on layer 15, net 3.3V11
- added copper zone on layer 15, net 3.3V3
- added copper zone on layer 15, net 3.3V4
- added copper zone on layer 15, net 3.3V5
- added copper zone on layer 15, net 3.3V6
- added copper zone on layer 15, net 3.3V7
- added copper zone on layer 15, net 3.3V8
- added copper zone on layer 15, net 3.3V9
- added copper zone on layer 1, net GND10
- added copper zone on layer 16, net GND10
- added copper zone on layer 2, net GND10
- added copper zone on layer 1, net GND11
- added copper zone on layer 16, net GND11
- added copper zone on layer 2, net GND11
- added copper zone on layer 1, net GND3
- added copper zone on layer 16, net GND3
- added copper zone on layer 2, net GND3
- added copper zone on layer 1, net GND4
- added copper zone on layer 16, net GND4
- added copper zone on layer 2, net GND4
- added copper zone on layer 1, net GND5
- added copper zone on layer 16, net GND5
- added copper zone on layer 2, net GND5
- added copper zone on layer 1, net GND6
- added copper zone on layer 16, net GND6
- added copper zone on layer 2, net GND6
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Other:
- board size 89.7 x 72.6 mm -> 106.7 x 203.2 mm
- board text added: "Route Out"
- board text added: "v10"
- board text removed: "v01"

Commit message: Change RGB jumper to NO
Won't violate the form factor standard by default this time!
Also update panel files
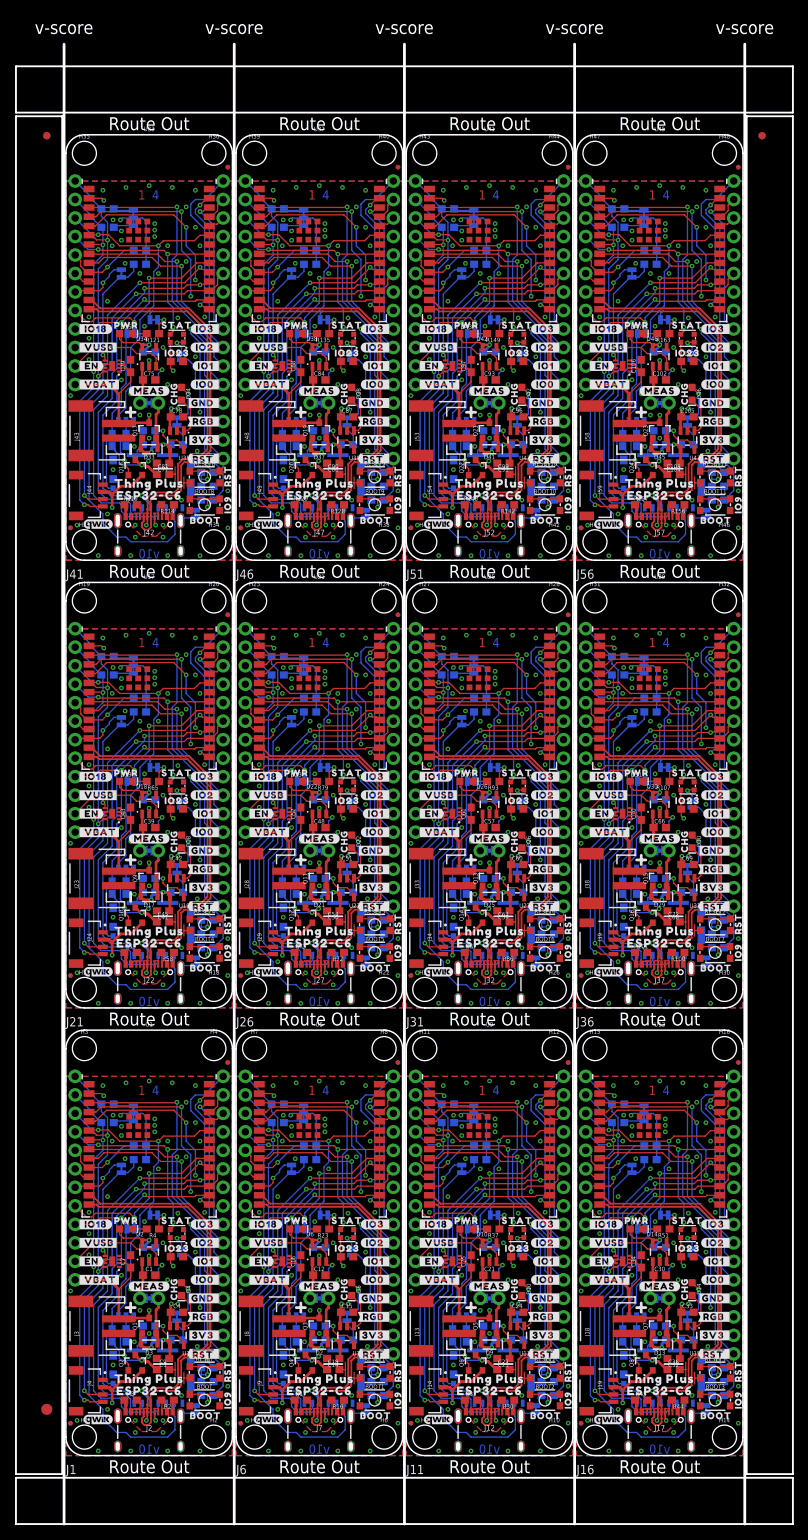
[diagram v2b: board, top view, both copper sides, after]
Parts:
- RGB, RGB1, RGB10, RGB11, RGB2, RGB3, RGB4, RGB5, RGB6, RGB7, RGB8, RGB9: value JUMPER-SMT_2_NC_TRACE_SILK -> JUMPER-SMT_2_NO_SILK; device SparkFun-Jumpers:SMT-JUMPER_2_NC_TRACE_SILK -> SparkFun-Jumpers:SMT-JUMPER_2_NO_SILK

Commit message: Change C6 to DNP
Rise time was slow, causing chip to run bootloader instead of booting from flash
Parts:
- C101, C11, C20, C29, C38, C47, C56, C6, C65, C74, C83, C92: value 0.1uF -> DNP
